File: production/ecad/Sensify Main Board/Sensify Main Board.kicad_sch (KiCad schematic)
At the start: 0 parts

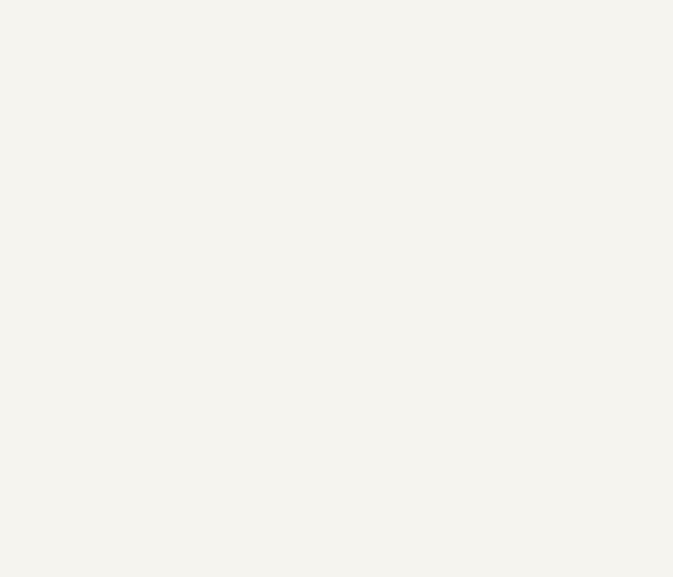
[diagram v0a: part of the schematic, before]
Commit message: Added Haptics kicad file to main board
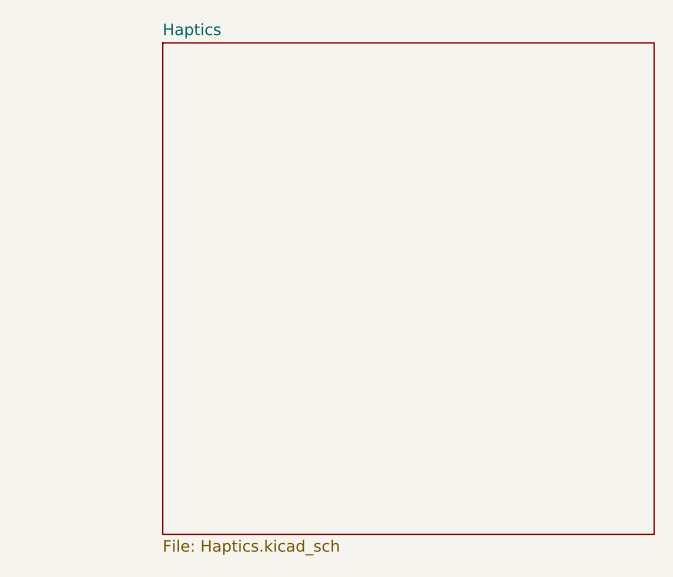
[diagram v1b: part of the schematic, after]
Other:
- added sheet Haptics (Haptics.kicad_sch)
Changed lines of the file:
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@@
+    )
+  )
+  (sheet (at 208.28 27.94) (size 54.61 54.61) (fields_autoplaced)
+    (stroke (width 0.1524) (type solid))
+    (fill (color 0 0 0 0.0000))
+    (property "Sheetname" "Haptics" (at 208.28 27.2284 0)
+      (effects (font (size 1.27 1.27)) (justify left bottom))
+    )
+    (property "Sheetfile" "Haptics.kicad_sch" (at 208.28 83.1346 0)
+      (effects (font (size 1.27 1.27)) (justify left top))
+    )
+    (instances
+      (project "Sensify Main Board"
+        (path "/9a7ba7c3-7d28-4a83-bdbc-38fbff59fcbe" (page "4"))
+      )
     )
   )

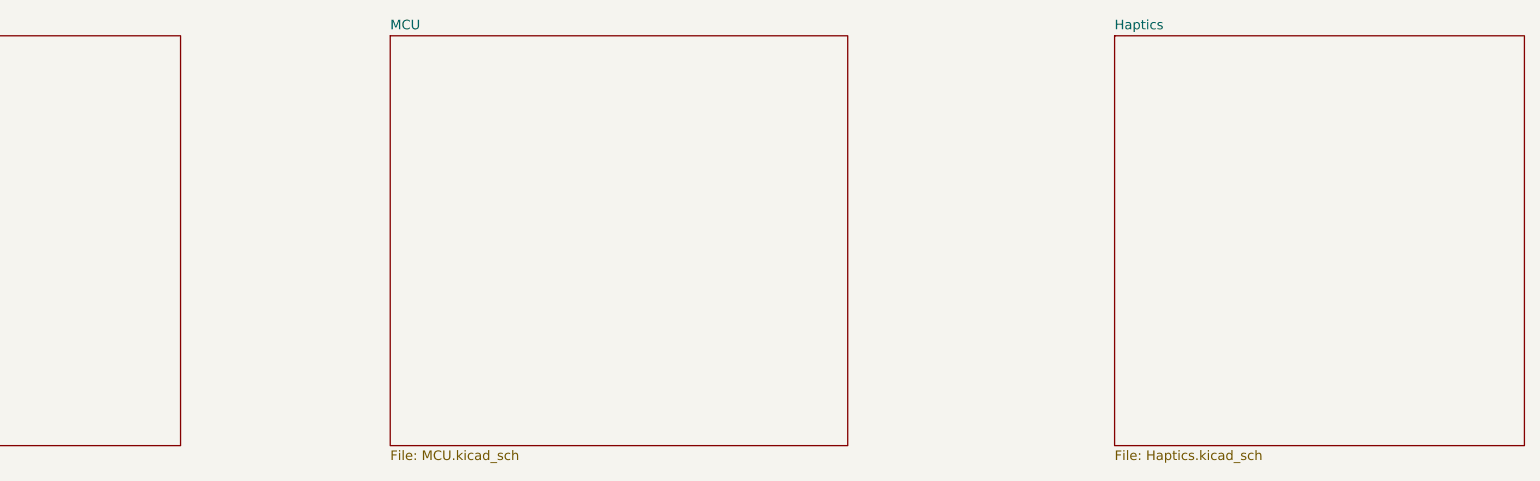
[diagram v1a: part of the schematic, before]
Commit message: Imported Sheet Pins
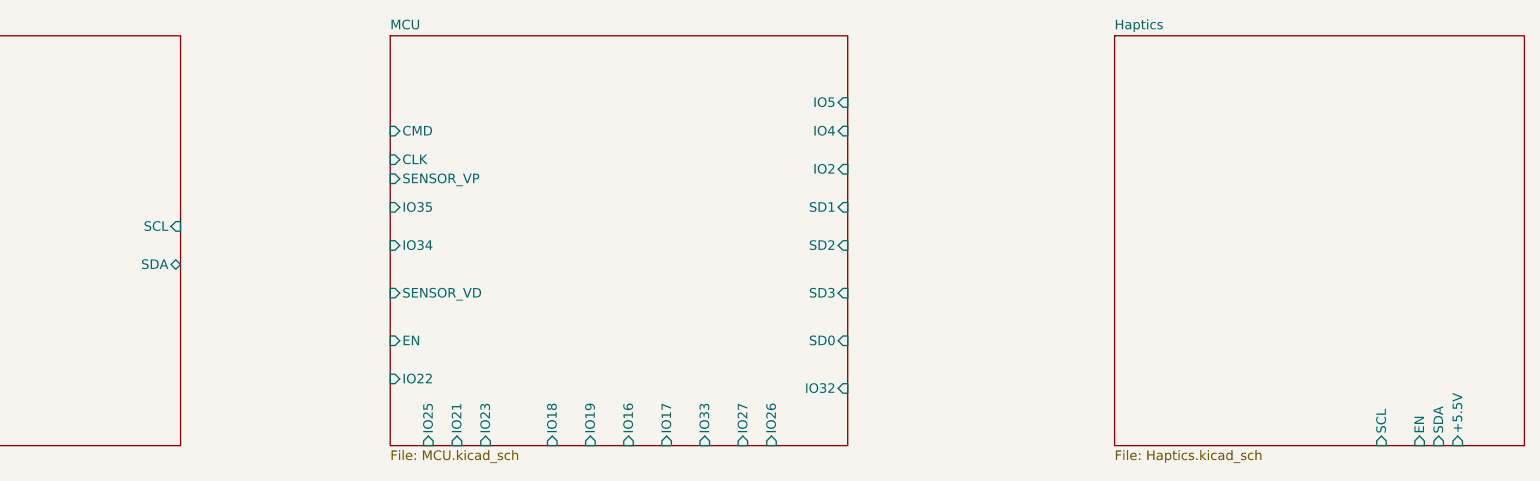
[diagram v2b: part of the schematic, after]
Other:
- sheet BMS ports: added SCL, SDA; removed none
- sheet Haptics ports: added +5.5V, EN, SCL, SDA; removed none
- sheet MCU ports: added CLK, CMD, EN, IO16, IO17, IO18, IO19, IO2, IO21, IO22, IO23, IO25, IO26, IO27, IO32, IO33, IO34, IO35, IO4, IO5, SD0, SD1, SD2, SD3, SENSOR_VD, SENSOR_VP; removed none
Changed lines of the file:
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@@
       (effects (font (size 1.27 1.27)) (justify left top))
+    )
+    (pin "SCL" input (at 83.82 53.34 0)
+      (effects (font (size 1.27 1.27)) (justify right))
+    )
+    (pin "SDA" bidirectional (at 83.82 58.42 0)
+      (effects (font (size 1.27 1.27)) (justify right))
     )
     (instances
@@
       (effects (font (size 1.27 1.27)) (justify left top))
     )
+    (pin "+5.5V" input (at 254 82.55 270)
+      (effects (font (size 1.27 1.27)) (justify left))
+    )
+    (pin "SDA" input (at 251.46 82.55 270)
+      (effects (font (size 1.27 1.27)) (justify left))
+    )
+    (pin "EN" input (at 248.92 82.55 270)
+      (effects (font (size 1.27 1.27)) (justify left))
+    )
+    (pin "SCL" input (at 243.84 82.55 270)
+      (effects (font (size 1.27 1.27)) (justify left))
+    )
     (instances
       (project "Sensify Main Board"
@@
       (effects (font (size 1.27 1.27)) (justify left top))
     )
+    (pin "IO5" input (at 172.72 36.83 0)
+      (effects (font (size 1.27 1.27)) (justify right))
+    )
+    (pin "IO4" input (at 172.72 40.64 0)
+      (effects (font (size 1.27 1.27)) (justify right))
+    )
+    (pin "IO2" input (at 172.72 45.72 0)
+      (effects (font (size 1.27 1.27)) (justify right))
+    )
+    (pin "SD1" input (at 172.72 50.8 0)
+      (effects (font (size 1.27 1.27)) (justify right))
+    )
+    (pin "SD2" input (at 172.72 55.88 0)
+      (effects (font (size 1.27 1.27)) (justify right))
+    )
+    (pin "SD3" input (at 172.72 62.23 0)
+      (effects (font (size 1.27 1.27)) (justify right))
+    )
+    (pin "SD0" input (at 172.72 68.58 0)
+      (effects (font (size 1.27 1.27)) (justify right))
+    )
+    (pin "IO32" input (at 172.72 74.93 0)
+      (effects (font (size 1.27 1.27)) (justify right))
+    )
+    (pin "IO26" input (at 162.56 82.55 270)
+      (effects (font (size 1.27 1.27)) (justify left))
+    )
+    (pin "IO27" input (at 158.75 82.55 270)
+      (effects (font (size 1.27 1.27)) (justify left))
+    )
+    (pin "IO33" input (at 153.67 82.55 270)
+      (effects (font (size 1.27 1.27)) (justify left))
+    )
+    (pin "IO17" input (at 148.59 82.55 270)
+      (effects (font (size 1.27 1.27)) (justify left))
+    )
+    (pin "IO16" input (at 143.51 82.55 270)
+      (effects (font (size 1.27 1.27)) (justify left))
+    )
+    (pin "IO19" input (at 138.43 82.55 270)
+      (effects (font (size 1.27 1.27)) (justify left))
+    )
+    (pin "IO18" input (at 133.35 82.55 270)
+      (effects (font (size 1.27 1.27)) (justify left))
+    )
+    (pin "IO23" input (at 124.46 82.55 270)
+      (effects (font (size 1.27 1.27)) (justify left))
+    )
+    (pin "IO21" input (at 120.65 82.55 270)
+      (effects (font (size 1.27 1.27)) (justify left))
+    )
+    (pin "IO25" input (at 116.84 82.55 270)
+      (effects (font (size 1.27 1.27)) (justify left))
+    )
+    (pin "IO22" input (at 111.76 73.66 180)
+      (effects (font (size 1.27 1.27)) (justify left))
+    )
+    (pin "EN" input (at 111.76 68.58 180)
+      (effects (font (size 1.27 1.27)) (justify left))
+    )
+    (pin "SENSOR_VD" input (at 111.76 62.23 180)
+      (effects (font (size 1.27 1.27)) (justify left))
+    )
+    (pin "IO34" input (at 111.76 55.88 180)
+      (effects (font (size 1.27 1.27)) (justify left))
+    )
+    (pin "IO35" input (at 111.76 50.8 180)
+      (effects (font (size 1.27 1.27)) (justify left))
+    )
+    (pin "SENSOR_VP" input (at 111.76 46.99 180)
+      (effects (font (size 1.27 1.27)) (justify left))
+    )
+    (pin "CLK" input (at 111.76 44.45 180)
+      (effects (font (size 1.27 1.27)) (justify left))
+    )
+    (pin "CMD" input (at 111.76 40.64 180)
+      (effects (font (size 1.27 1.27)) (justify left))
+    )
     (instances

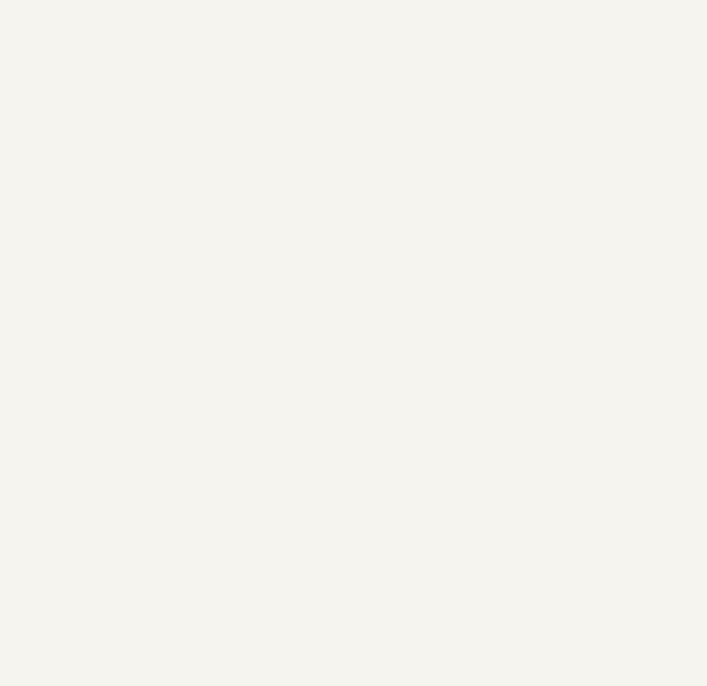
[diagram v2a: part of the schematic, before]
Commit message: IMU
Added an IMU sheet and connected IMU to stuff
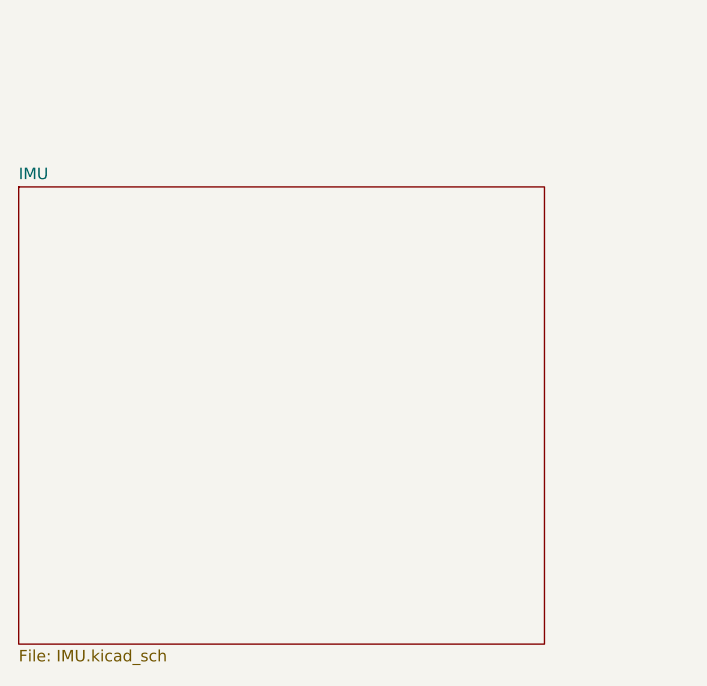
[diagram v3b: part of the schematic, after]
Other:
- added sheet IMU (IMU.kicad_sch)
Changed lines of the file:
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@@
+    )
+  )
+  (sheet (at 26.67 115.57) (size 58.42 50.8) (fields_autoplaced)
+    (stroke (width 0.1524) (type solid))
+    (fill (color 0 0 0 0.0000))
+    (property "Sheetname" "IMU" (at 26.67 114.8584 0)
+      (effects (font (size 1.27 1.27)) (justify left bottom))
+    )
+    (property "Sheetfile" "IMU.kicad_sch" (at 26.67 166.9546 0)
+      (effects (font (size 1.27 1.27)) (justify left top))
+    )
+    (instances
+      (project "Sensify Main Board"
+        (path "/9a7ba7c3-7d28-4a83-bdbc-38fbff59fcbe" (page "5"))
+      )
     )
   )

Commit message: "Improved MCU Schematic"
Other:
- sheet Haptics ports: added +5V; removed none
- sheet IMU ports: added 3.3V, GND, IMU_INTR1, IMU_INTR2, SCL, SDA; removed none
- sheet MCU ports: added 3V3, 5V, GND, INTERRUPT1_IMU, INTERRUPT2_IMU, MCU_WAKEUP, SCL, SDA; removed CLK, CMD, EN, IO16, IO17, IO18, IO19, IO2, IO21, IO22, IO23, IO25, IO26, IO27, IO32, IO33, IO34, IO35, IO4, IO5, SD0, SD1, SD2, SD3, SENSOR_VD, SENSOR_VP
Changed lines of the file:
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@@
 (kicad_sch (version 20230121) (generator eeschema)
   (paper "A4")
+  (junction (at 137.16 19.05) (diameter 0) (color 0 0 0 0)
+  )
+  (junction (at 143.51 15.24) (diameter 0) (color 0 0 0 0)
+  )
+  (wire (pts (xy 143.51 15.24) (xy 185.42 15.24))
+    (stroke (width 0) (type default))
+  )
+  (wire (pts (xy 85.09 128.27) (xy 106.68 128.27))
+    (stroke (width 0) (type default))
+  )
+  (wire (pts (xy 83.82 53.34) (xy 93.98 53.34))
+    (stroke (width 0) (type default))
+  )
+  (wire (pts (xy 179.07 19.05) (xy 179.07 137.16))
+    (stroke (width 0) (type default))
+  )
+  (wire (pts (xy 106.68 69.85) (xy 111.76 69.85))
+    (stroke (width 0) (type default))
+  )
+  (wire (pts (xy 85.09 137.16) (xy 179.07 137.16))
+    (stroke (width 0) (type default))
+  )
+  (wire (pts (xy 85.09 142.24) (xy 185.42 142.24))
+    (stroke (width 0) (type default))
+  )
+  (wire (pts (xy 85.09 123.19) (xy 102.87 123.19))
+    (stroke (width 0) (type default))
+  )
+  (wire (pts (xy 83.82 58.42) (xy 97.79 58.42))
+    (stroke (width 0) (type default))
+  )
+  (wire (pts (xy 106.68 69.85) (xy 106.68 128.27))
+    (stroke (width 0) (type default))
+  )
+  (wire (pts (xy 93.98 19.05) (xy 93.98 53.34))
+    (stroke (width 0) (type default))
+  )
+  (wire (pts (xy 143.51 15.24) (xy 143.51 27.94))
+    (stroke (width 0) (type default))
+  )
+  (wire (pts (xy 102.87 66.04) (xy 111.76 66.04))
+    (stroke (width 0) (type default))
+  )
+  (wire (pts (xy 97.79 15.24) (xy 143.51 15.24))
+    (stroke (width 0) (type default))
+  )
+  (wire (pts (xy 102.87 66.04) (xy 102.87 123.19))
+    (stroke (width 0) (type default))
+  )
+  (wire (pts (xy 137.16 19.05) (xy 137.16 27.94))
+    (stroke (width 0) (type default))
+  )
+  (wire (pts (xy 93.98 19.05) (xy 137.16 19.05))
+    (stroke (width 0) (type default))
+  )
+  (wire (pts (xy 137.16 19.05) (xy 179.07 19.05))
+    (stroke (width 0) (type default))
+  )
+  (wire (pts (xy 185.42 15.24) (xy 185.42 142.24))
+    (stroke (width 0) (type default))
+  )
+  (wire (pts (xy 97.79 15.24) (xy 97.79 58.42))
+    (stroke (width 0) (type default))
+  )
   (sheet (at 26.67 27.94) (size 57.15 54.61) (fields_autoplaced)
     (stroke (width 0.1524) (type solid))
@@
       (effects (font (size 1.27 1.27)) (justify left top))
     )
-    (pin "+5.5V" input (at 254 82.55 270)
+    (pin "+5.5V" input (at 208.28 67.31 180)
       (effects (font (size 1.27 1.27)) (justify left))
     )
-    (pin "SDA" input (at 251.46 82.55 270)
+    (pin "SDA" input (at 208.28 59.69 180)
       (effects (font (size 1.27 1.27)) (justify left))
     )
-    (pin "EN" input (at 248.92 82.55 270)
+    (pin "EN" input (at 208.28 52.07 180)
       (effects (font (size 1.27 1.27)) (justify left))
     )
-    (pin "SCL" input (at 243.84 82.55 270)
+    (pin "SCL" input (at 208.28 45.72 180)
+      (effects (font (size 1.27 1.27)) (justify left))
+    )
+    (pin "+5V" input (at 208.28 38.1 180)
       (effects (font (size 1.27 1.27)) (justify left))
     )
@@
       (effects (font (size 1.27 1.27)) (justify left top))
     )
+    (pin "3.3V" bidirectional (at 43.18 115.57 90)
+      (effects (font (size 1.27 1.27)) (justify right))
+    )
+    (pin "IMU_INTR2" bidirectional (at 85.09 123.19 0)
+      (effects (font (size 1.27 1.27)) (justify right))
+    )
+    (pin "SCL" output (at 85.09 137.16 0)
+      (effects (font (size 1.27 1.27)) (justify right))
+    )
+    (pin "IMU_INTR1" bidirectional (at 85.09 128.27 0)
+      (effects (font (size 1.27 1.27)) (justify right))
+    )
+    (pin "SDA" bidirectional (at 85.09 142.24 0)
+      (effects (font (size 1.27 1.27)) (justify right))
+    )
+    (pin "GND" bidirectional (at 52.07 115.57 90)
+      (effects (font (size 1.27 1.27)) (justify right))
+    )
     (instances
       (project "Sensify Main Board"
@@
       (effects (font (size 1.27 1.27)) (justify left top))
     )
-    (pin "IO5" input (at 172.72 36.83 0)
+    (pin "5V" input (at 111.76 38.1 180)
+      (effects (font (size 1.27 1.27)) (justify left))
+    )
+    (pin "GND" bidirectional (at 111.76 44.45 180)
+      (effects (font (size 1.27 1.27)) (justify left))
+    )
+    (pin "3V3" input (at 111.76 50.8 180)
+      (effects (font (size 1.27 1.27)) (justify left))
+    )
+    (pin "MCU_WAKEUP" input (at 111.76 58.42 180)
+      (effects (font (size 1.27 1.27)) (justify left))
+    )
+    (pin "INTERRUPT2_IMU" bidirectional (at 111.76 66.04 180)
+      (effects (font (size 1.27 1.27)) (justify left))
+    )
+    (pin "SCL" bidirectional (at 137.16 27.94 90)
       (effects (font (size 1.27 1.27)) (justify right))
     )
-    (pin "IO4" input (at 172.72 40.64 0)
+    (pin "SDA" bidirectional (at 143.51 27.94 90)
       (effects (font (size 1.27 1.27)) (justify right))
     )
-    (pin "IO2" input (at 172.72 45.72 0)
-      (effects (font (size 1.27 1.27)) (justify right))
-    )
-    (pin "SD1" input (at 172.72 50.8 0)
-      (effects (font (size 1.27 1.27)) (justify right))
-    )
-    (pin "SD2" input (at 172.72 55.88 0)
-      (effects (font (size 1.27 1.27)) (justify right))
-    )
-    (pin "SD3" input (at 172.72 62.23 0)
-      (effects (font (size 1.27 1.27)) (justify right))
-    )
-    (pin "SD0" input (at 172.72 68.58 0)
-      (effects (font (size 1.27 1.27)) (justify right))
-    )
-    (pin "IO32" input (at 172.72 74.93 0)
-      (effects (font (size 1.27 1.27)) (justify right))
-    )
-    (pin "IO26" input (at 162.56 82.55 270)
+    (pin "INTERRUPT1_IMU" bidirectional (at 111.76 69.85 180)
       (effects (font (size 1.27 1.27)) (justify left))
     )
-    (pin "IO27" input (at 158.75 82.55 270)
-      (effects (font (size 1.27 1.27)) (justify left))
-    )
-    (pin "IO33" input (at 153.67 82.55 270)
-      (effects (font (size 1.27 1.27)) (justify left))
-    )
-    (pin "IO17" input (at 148.59 82.55 270)
-      (effects (font (size 1.27 1.27)) (justify left))
-    )
-    (pin "IO16" input (at 143.51 82.55 270)
-      (effects (font (size 1.27 1.27)) (justify left))
-    )
-    (pin "IO19" input (at 138.43 82.55 270)
-      (effects (font (size 1.27 1.27)) (justify left))
-    )
-    (pin "IO18" input (at 133.35 82.55 270)
-      (effects (font (size 1.27 1.27)) (justify left))
-    )
-    (pin "IO23" input (at 124.46 82.55 270)
-      (effects (font (size 1.27 1.27)) (justify left))
-    )
-    (pin "IO21" input (at 120.65 82.55 270)
-      (effects (font (size 1.27 1.27)) (justify left))
-    )
-    (pin "IO25" input (at 116.84 82.55 270)
-      (effects (font (size 1.27 1.27)) (justify left))
-    )
-    (pin "IO22" input (at 111.76 73.66 180)
-      (effects (font (size 1.27 1.27)) (justify left))
-    )
-    (pin "EN" input (at 111.76 68.58 180)
-      (effects (font (size 1.27 1.27)) (justify left))
-    )
-    (pin "SENSOR_VD" input (at 111.76 62.23 180)
-      (effects (font (size 1.27 1.27)) (justify left))
-    )
-    (pin "IO34" input (at 111.76 55.88 180)
-      (effects (font (size 1.27 1.27)) (justify left))
-    )
-    (pin "IO35" input (at 111.76 50.8 180)
-      (effects (font (size 1.27 1.27)) (justify left))
-    )
-    (pin "SENSOR_VP" input (at 111.76 46.99 180)
-      (effects (font (size 1.27 1.27)) (justify left))
-    )
-    (pin "CLK" input (at 111.76 44.45 180)
-      (effects (font (size 1.27 1.27)) (justify left))
-    )
-    (pin "CMD" input (at 111.76 40.64 180)
-      (effects (font (size 1.27 1.27)) (justify left))
-    )
